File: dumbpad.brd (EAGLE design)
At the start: 97 x 78.5 mm, 44 parts

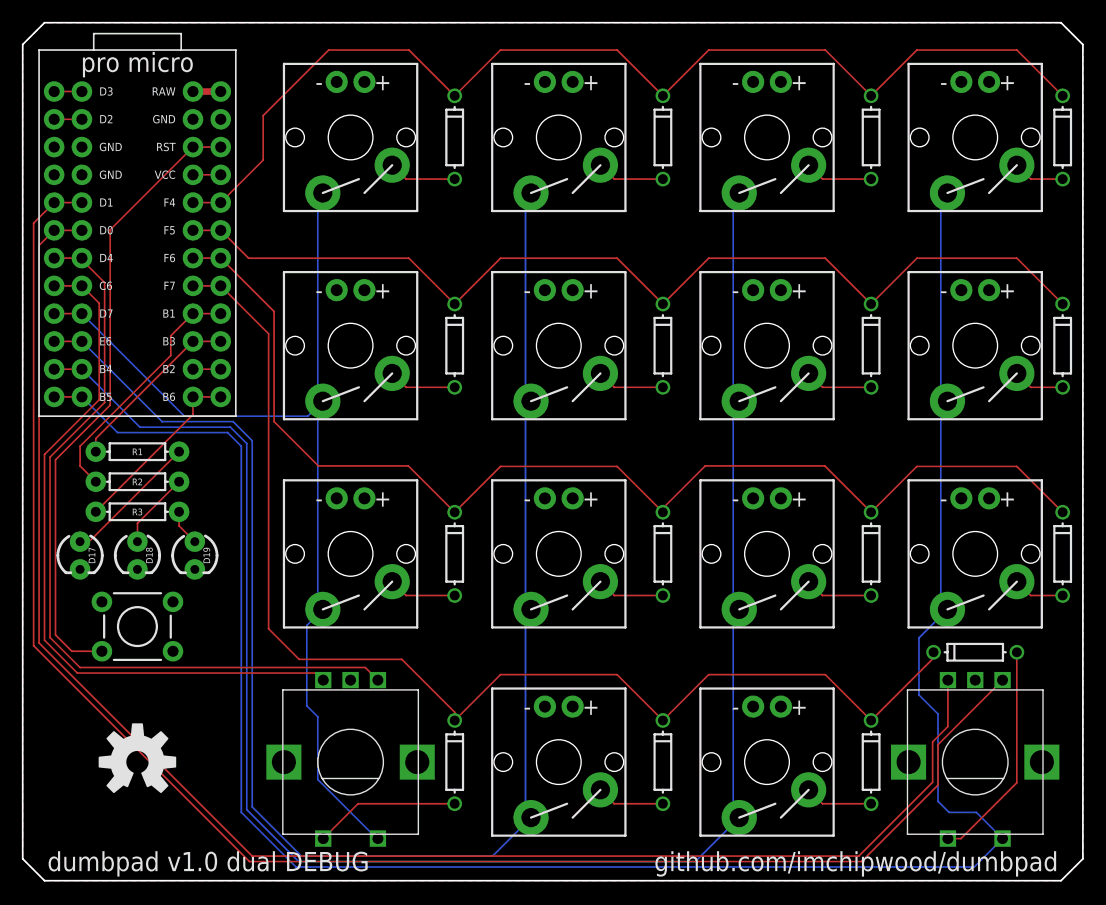
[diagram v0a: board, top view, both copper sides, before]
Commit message: added mounting holes
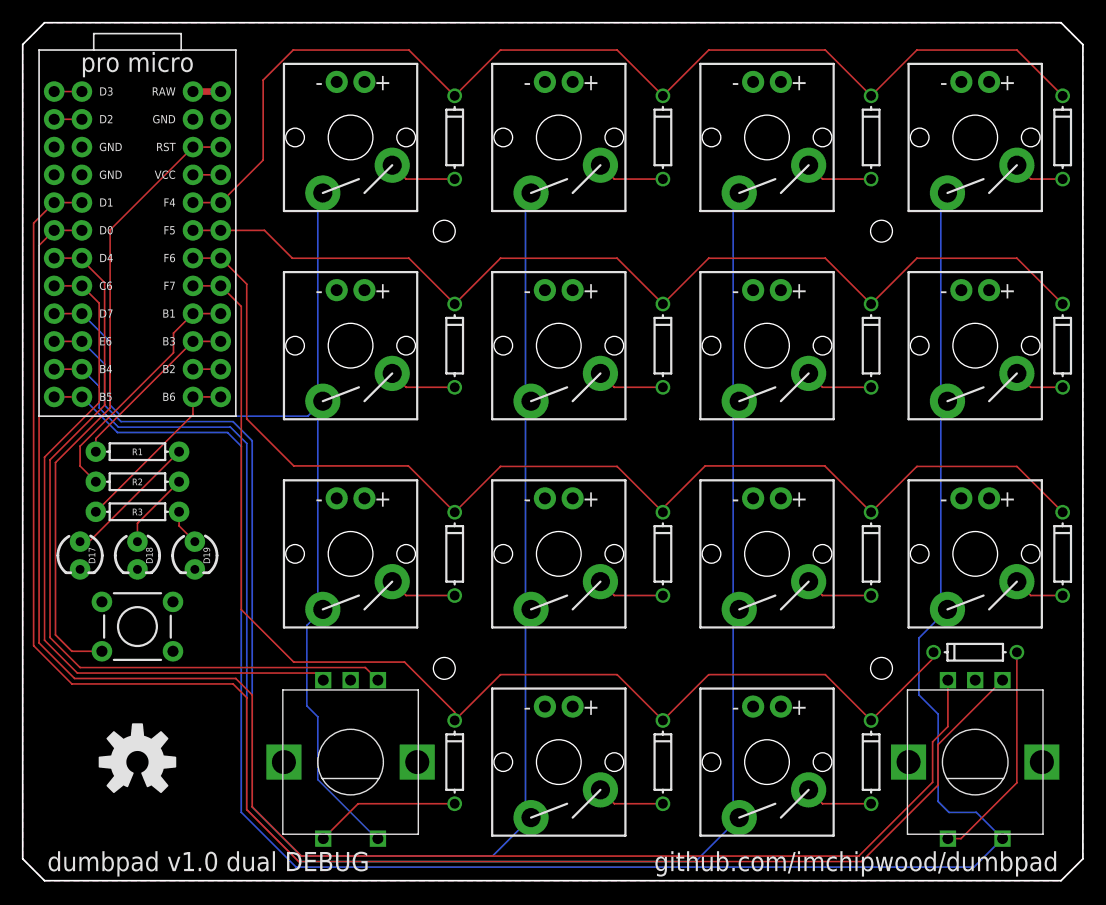
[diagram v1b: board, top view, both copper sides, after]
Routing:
- net ENCODER1_L0: track 149.7 -> 155.7 mm
- net ENCODER1_L1: track 143.4 -> 149.4 mm
- net COL0: track 91.6 -> 95.0 mm
- net COL1: track 142.6 -> 144.8 mm
- net ROW0: track 99.9 -> 101.8 mm
- net ROW2: track 105.7 -> 107.0 mm
- net COL2: track 161.2 -> 162.3 mm
